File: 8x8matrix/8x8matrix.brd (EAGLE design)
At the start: 60.4 x 60.5 mm, 21 parts

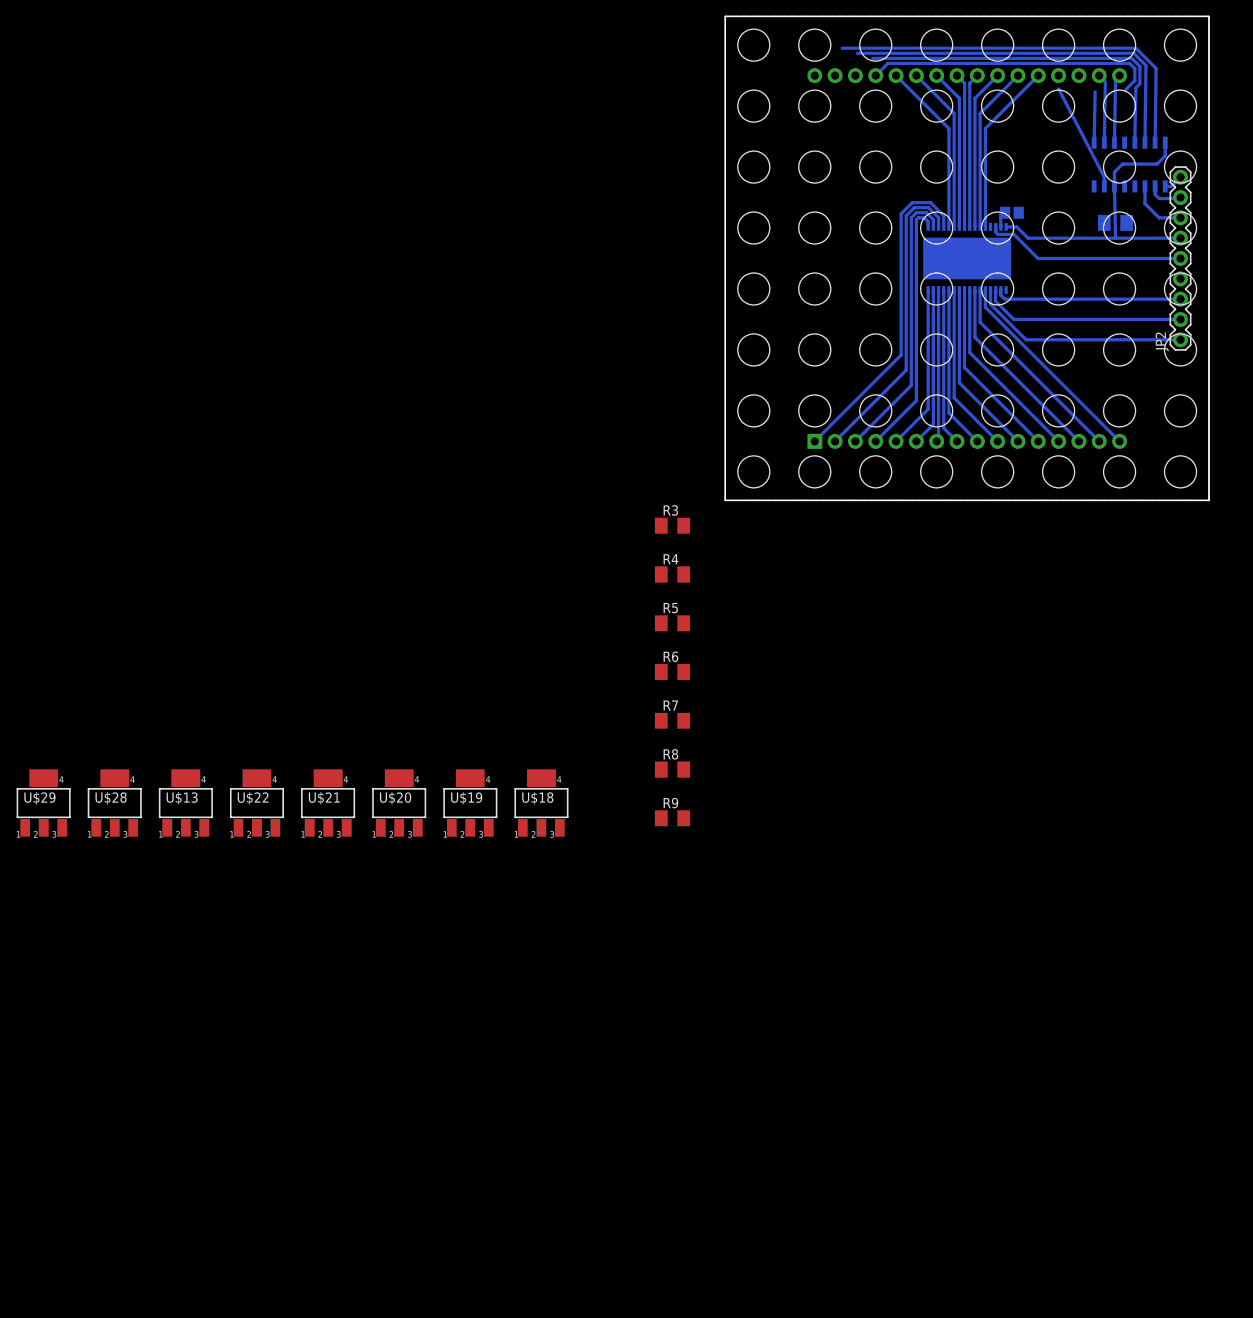
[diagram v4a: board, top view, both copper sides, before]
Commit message: tried with regular SOT23 PNPs
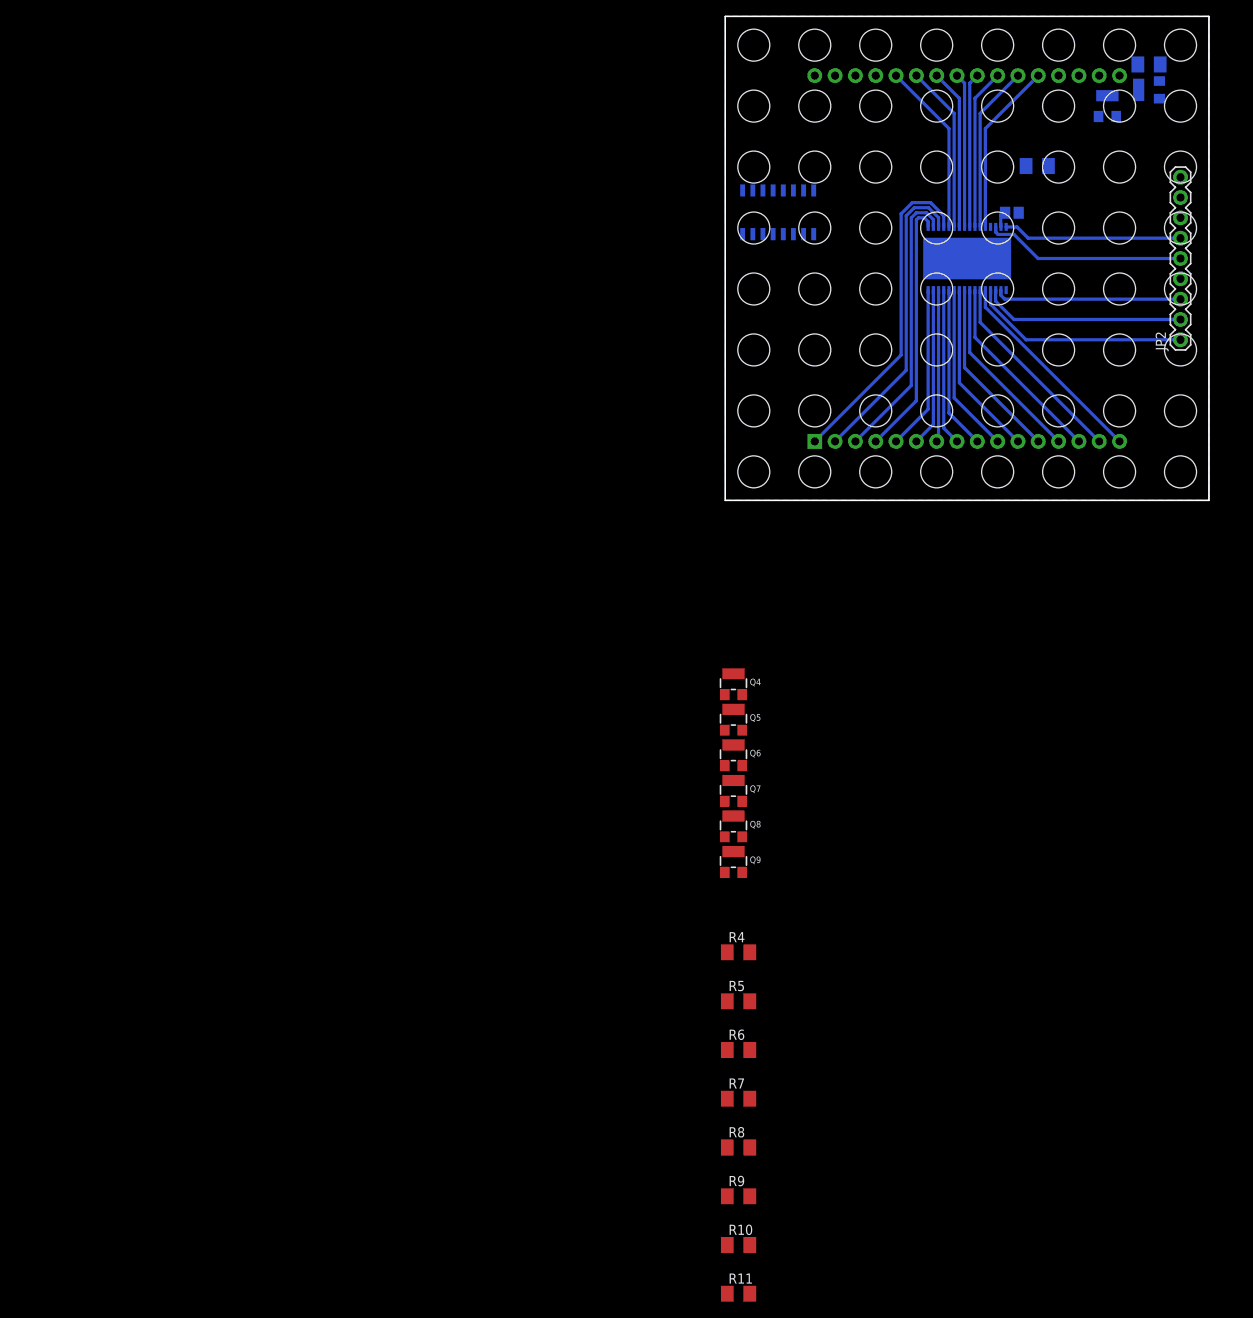
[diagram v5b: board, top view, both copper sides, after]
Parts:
- removed U$13, U$18, U$19, U$20, U$21, U$22, U$28, U$29: FZTA92, mylib:SOT223
- added Q1, Q2, Q4, Q5, Q6, Q7, Q8, Q9: (no value), microbuilder:SOT23-W
- added R10, R11: 0R, resistor:M1206
- moved R3 82.9 mm to (53.0, 54.5), flipped to the bottom, turned to 180 degrees
- moved R9 48.0 mm to (1.65, -87.0)
- moved R4 48.0 mm to (1.65, -56.5)
- moved R5 48.0 mm to (1.65, -62.6)
- moved R7 48.0 mm to (1.65, -74.8)
- moved R8 48.0 mm to (1.65, -80.9)
- moved R6 48.0 mm to (1.65, -68.7)
- moved U$9 44.4 mm to (6.60, 35.9), turned to 180 degrees
- moved R2 12.1 mm to (39.0, 41.8)
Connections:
- new net N$52: Q9.3, U$1.P32
- net 5.0V: now also Q1.2, Q2.2, Q4.2, Q5.2, Q6.2, Q7.2, Q8.2, Q9.2; no longer U$13.3, U$18.3, U$19.3, U$20.3, U$21.3, U$22.3, U$28.3, U$29.3
- net N$25: no longer U$13.1
- net N$26: now also R7.1
- net N$28: now also Q1.3, U$1.P17; no longer R5.2, U$18.1
- net N$29: now also R5.1; no longer R7.1
- net N$30: now also R4.1; no longer R8.1
- net N$31: now also R3.1; no longer R9.1
- net N$32: now also Q4.1, R5.2; no longer U$1.P29, U$13.2, U$13.4
- net N$33: no longer R5.1
- net N$34: now also R10.1; no longer R4.1
- net N$35: now also R11.1; no longer R3.1
- net N$39: now also Q7.1, R9.2; no longer R7.2, U$20.1
- net N$40: now also Q8.1, R10.2; no longer R8.2, U$21.1
- net N$41: now also Q1.1, R3.2; no longer R9.2, U$22.1
- net N$42: now also Q2.1, R4.2; no longer U$1.P30, U$18.2, U$18.4
- net N$43: now also Q5.1, R6.2, R7.2; no longer U$1.P17, U$22.2, U$22.4
- net N$44: now also Q2.3; no longer U$21.2, U$21.4
- net N$45: now also Q6.1, R8.2; no longer R6.2, U$19.1
- net N$46: now also Q9.1, R11.2; no longer U$1.P19, U$20.2, U$20.4
- net N$47: now also Q5.3; no longer U$19.2, U$19.4
- net N$48: now also Q4.3, U$1.P19; no longer R4.2, U$28.1
- net N$49: now also Q6.3, U$1.P29; no longer R3.2, U$29.1
- net N$50: now also Q7.3, U$1.P30; no longer U$1.P31, U$28.2, U$28.4
- net N$51: now also Q8.3, U$1.P31; no longer U$1.P32, U$29.2, U$29.4
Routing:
- net N$35: track 49.6 -> 0.00 mm
- net N$34: track 46.4 -> 0.00 mm
- net N$33: track 43.6 -> 0.00 mm
- net N$32: track 36.4 -> 0.00 mm
- net 5.0V: track 39.5 -> 22.4 mm
- net N$26: track 13.6 -> 0.00 mm
- net N$31: track 7.88 -> 0.00 mm
- net N$30: track 7.62 -> 0.00 mm
- net N$38: track 7.34 -> 0.00 mm
- net N$29: track 6.35 -> 0.00 mm
- net N$37: track 4.45 -> 0.00 mm
- net N$36: track 2.38 -> 0.00 mm

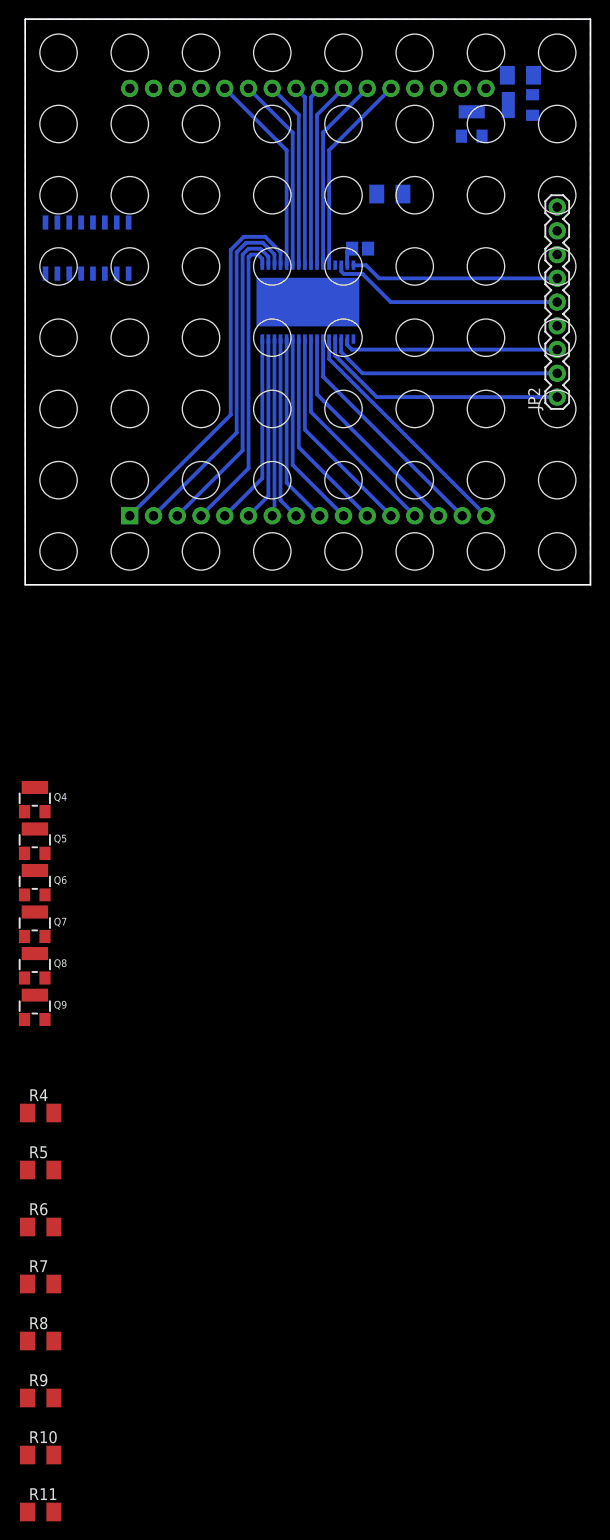
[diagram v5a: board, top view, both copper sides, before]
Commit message: tried with BCR198S pnp arrays
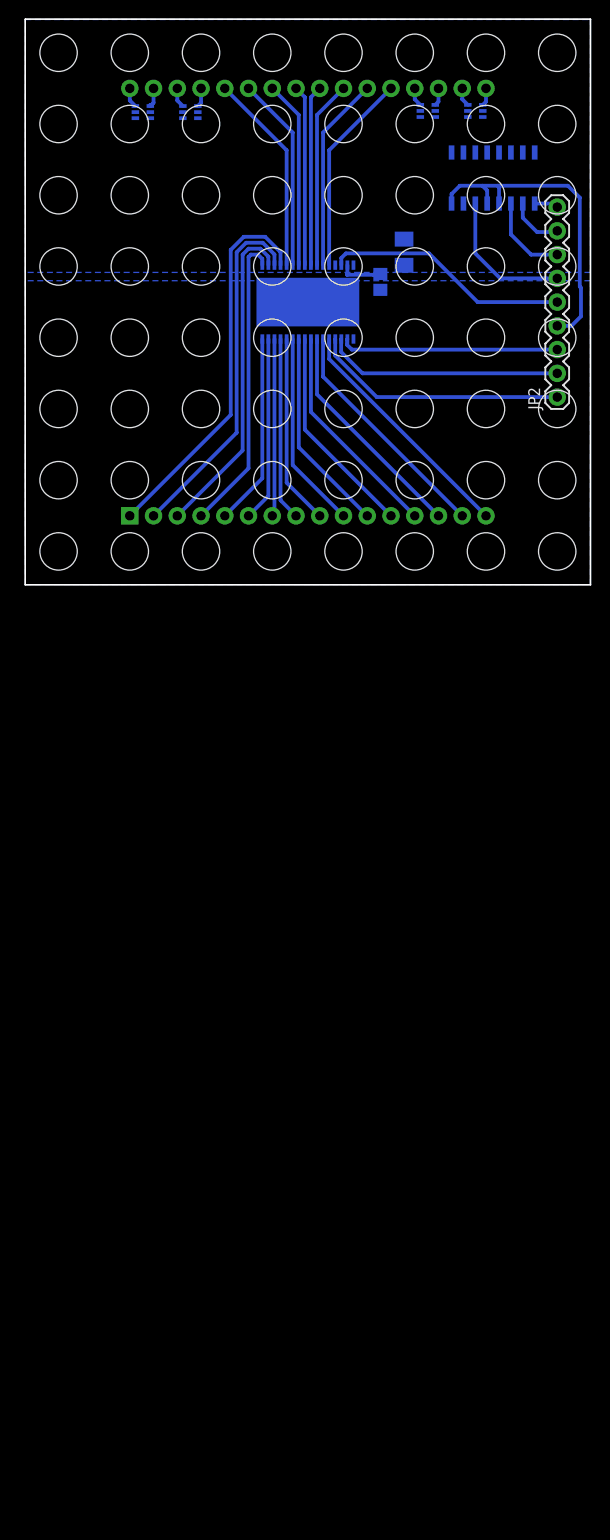
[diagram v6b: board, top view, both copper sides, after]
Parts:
- removed Q1, Q2, Q4, Q5, Q6, Q7, Q8, Q9: (no value), microbuilder:SOT23-W
- removed R10, R11, R3, R4, R5, R6, R7, R8, R9: 0R, resistor:M1206
- added U$13, U$17, U$18, U$19: BCR198S, mylib:SOT363_PHILIPS
- moved U$9 44.1 mm to (50.0, 43.6), turned to 0 degrees
- moved R2 6.41 mm to (40.5, 35.6), turned to 270 degrees
- moved R1 4.16 mm to (38.0, 32.4), turned to 90 degrees
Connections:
- removed net N$42: Q2.1, R4.2
- removed net N$43: Q5.1, R6.2, R7.2
- removed net N$44: Q2.3, U$1.P18
- removed net N$45: Q6.1, R8.2
- removed net N$46: Q9.1, R11.2
- removed net N$48: Q4.3, U$1.P19
- removed net N$49: Q6.3, U$1.P29
- removed net N$51: Q8.3, U$1.P31
- net 5.0V: now also R2.1, R2.2, U$13.1, U$13.6, U$17.1, U$17.6, U$18.1, U$18.6, U$19.6; no longer Q1.2, Q2.2, Q4.2, Q5.2, Q6.2, Q7.2, Q8.2, Q9.2
- net GND: no longer R2.1, R2.2
- net N$25: now also U$18.2
- net N$26: now also U$17.5; no longer R6.1, R7.1
- net N$28: now also U$1.P19, U$17.4; no longer Q1.3, U$1.P17
- net N$29: now also U$17.2; no longer R5.1
- net N$30: now also U$13.5; no longer R4.1
- net N$31: now also U$13.2; no longer R3.1
- net N$32: now also U$1.P18, U$13.3; no longer Q4.1, R5.2
- net N$33: now also U$18.5
- net N$34: now also U$19.2; no longer R10.1
- net N$35: now also U$19.5; no longer R11.1
- net N$39: now also U$1.P17, U$13.4; no longer Q7.1, R9.2
- net N$40: now also U$1.P29, U$18.4; no longer Q8.1, R10.2
- net N$41: now also U$1.P31, U$19.4; no longer Q1.1, R3.2
- net N$47: now also U$17.3; no longer Q5.3
- net N$50: now also U$18.3; no longer Q7.3
- net N$52: now also U$19.3; no longer Q9.3
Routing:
- net GND: track 0.00 -> 35.4 mm
- net N$38: track 0.00 -> 9.15 mm
- net 5.0V: track 22.4 -> 15.2 mm
- net N$37: track 0.00 -> 5.89 mm
- net N$36: track 0.00 -> 2.57 mm
- net N$27: track 2.18 -> 4.60 mm
- net N$41: track 0.00 -> 2.16 mm
- net N$50: track 0.00 -> 2.14 mm
- net N$52: track 0.00 -> 2.14 mm
- net N$40: track 0.00 -> 2.03 mm
- net N$47: track 0.00 -> 2.01 mm
- net N$32: track 0.00 -> 2.01 mm
- net N$39: track 0.00 -> 1.91 mm
- net N$28: track 0.00 -> 1.91 mm
- net XLAT: track 25.1 -> 26.2 mm
- added copper zone on layer 16, net 5.0V

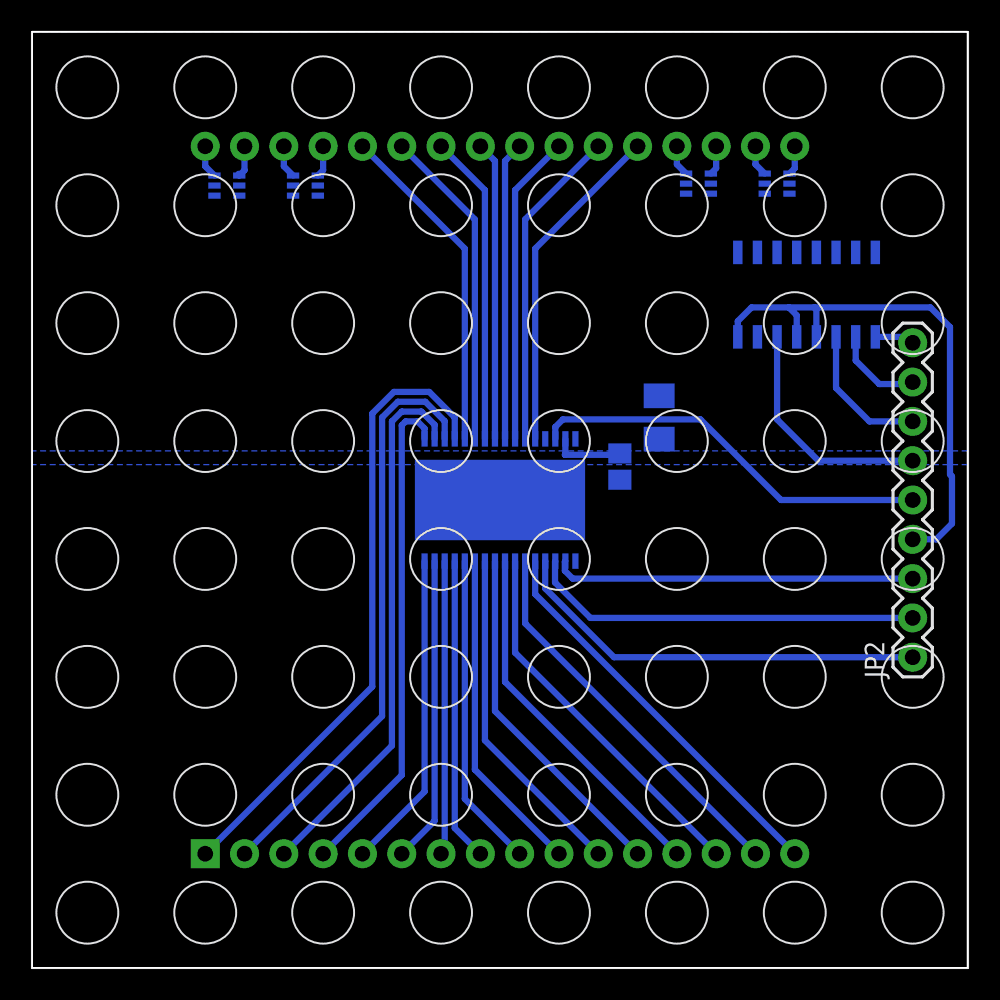
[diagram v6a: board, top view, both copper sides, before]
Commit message: found something that works: IRF7104
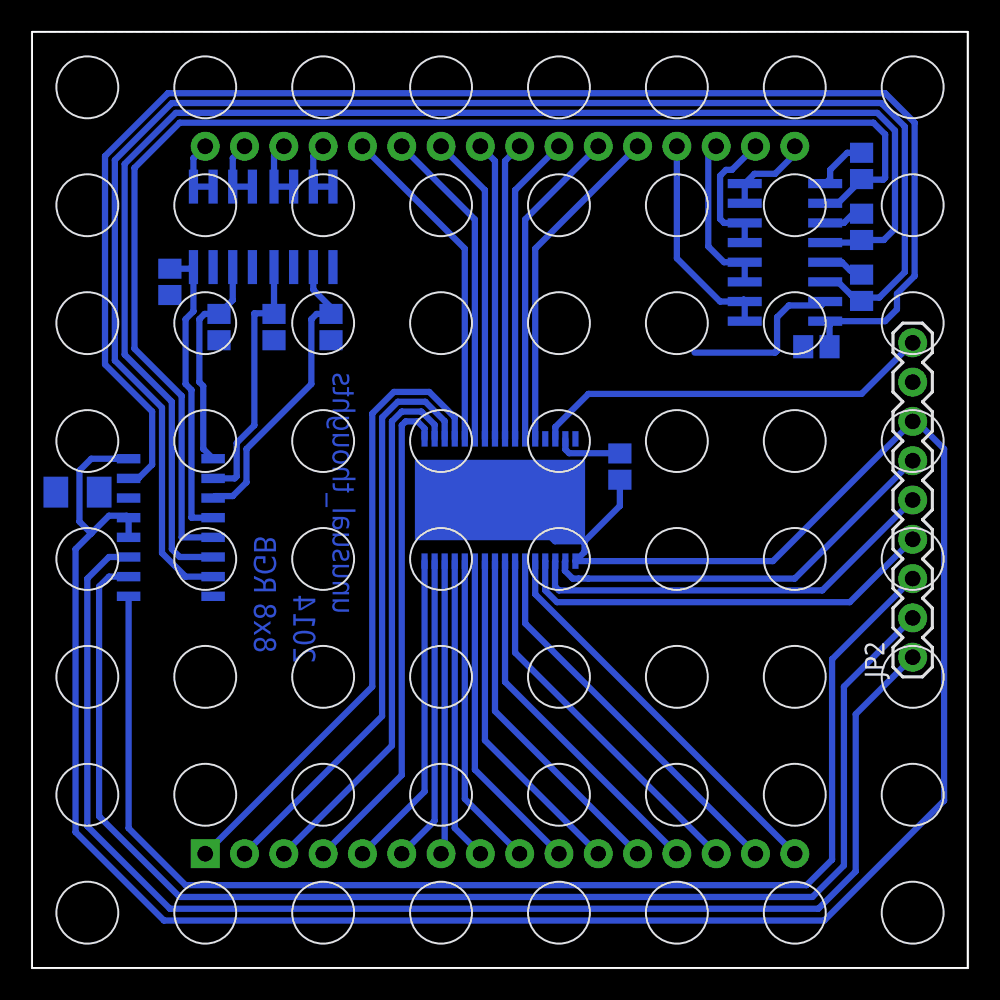
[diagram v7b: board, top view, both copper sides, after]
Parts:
- removed U$13, U$17, U$18, U$19: BCR198S, mylib:SOT363_PHILIPS
- added R10, R3, R4, R5, R6, R7, R8, R9: (no value), resistor:R0805
- added U$28, U$29, U$30, U$31: IRF7104, mylib:SOIC8
- R1: value (none) -> 3.3k
- moved U$9 43.7 mm to (9.02, 28.4), turned to 90 degrees
- moved R2 37.9 mm to (2.92, 30.7), turned to 180 degrees
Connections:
- removed net N$25: U$18.2, U$9.12
- removed net N$26: U$17.5, U$9.7
- removed net N$29: U$17.2, U$9.9
- removed net N$30: U$13.5, U$9.10
- removed net N$31: U$13.2, U$9.11
- removed net N$33: U$18.5, U$9.13
- removed net N$34: U$19.2, U$9.14
- removed net N$35: U$19.5, U$9.15
- removed net N$47: U$1.P20, U$17.3
- new net N$42: U$1.P20, U$29.5, U$29.6
- new net Y0: R5.1, U$29.2, U$9.15
- new net Y1: R4.1, U$28.4, U$9.14
- new net Y2: R3.1, U$28.2, U$9.13
- new net Y3: R10.1, U$31.4, U$9.12
- new net Y4: R7.1, U$30.2, U$9.11
- new net Y5: R8.1, U$30.4, U$9.10
- new net Y6: R9.1, U$31.2, U$9.9
- new net Y7: R6.1, U$29.4, U$9.7
- net 5.0V: now also JP2.8, R10.2, R3.2, R4.2, R5.2, R6.2, R7.2, R8.2, R9.2, U$28.1, U$28.3, U$29.1, U$29.3, U$30.1, U$30.3, U$31.1, U$31.3; no longer JP2.6, U$13.1, U$13.6, U$17.1, U$17.6, U$18.1, U$18.6, U$19.6
- net BLANK: now also JP2.6; no longer JP2.3
- net GND: now also JP2.7; no longer JP2.4
- net N$28: now also U$29.7, U$29.8; no longer U$17.4
- net N$32: now also U$28.5, U$28.6; no longer U$13.3
- net N$36: now also JP2.3; no longer JP2.9
- net N$37: now also JP2.2; no longer JP2.8
- net N$38: now also JP2.1; no longer JP2.7
- net N$39: now also U$28.7, U$28.8; no longer U$13.4
- net N$40: now also U$30.7, U$30.8; no longer U$18.4
- net N$41: now also U$31.7, U$31.8; no longer U$19.4
- net N$50: now also U$30.5, U$30.6; no longer U$18.3
- net N$52: now also U$31.5, U$31.6; no longer U$19.3
- net SCLK: now also JP2.5; no longer JP2.2
- net SIN: now also JP2.4; no longer JP2.1
- net XLAT: now also JP2.9; no longer JP2.5
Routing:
- net GND: track 35.4 -> 158.5 mm
- net Y0: track 0.00 -> 99.7 mm
- net Y7: track 0.00 -> 97.2 mm
- net Y1: track 0.00 -> 91.9 mm
- net Y2: track 0.00 -> 84.5 mm
- net N$36: track 2.57 -> 83.0 mm
- net N$37: track 5.89 -> 86.0 mm
- net N$38: track 9.15 -> 87.5 mm
- net Y4: track 0.00 -> 20.3 mm
- net Y3: track 0.00 -> 19.7 mm
- net Y5: track 0.00 -> 16.9 mm
- net Y6: track 0.00 -> 14.2 mm
- net N$42: track 0.00 -> 14.2 mm
- net N$28: track 1.91 -> 10.7 mm
- net N$32: track 2.01 -> 8.84 mm
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- removed copper zone on layer 16, net GND
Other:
- board text added: "2014"
- board text added: "8x8 RGB"
- board text added: "unusual_thoughts"

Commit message: changed 238 to 138
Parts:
- U$9: value CD74HC238M -> 74HC138D
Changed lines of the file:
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@@
 <element name="U$14" library="TLC5947" package="HTSSOP32DAP" value="TLC5947DAP" x="30.226" y="30.226" rot="MR0"/>
 <element name="R1" library="resistor" package="R0805" value="3.3k" x="37.973" y="32.385" rot="MR90"/>
-<element name="U$9" library="mylib" package="SO-16" value="CD74HC238M" x="9.017" y="28.448" rot="MR90"/>
+<element name="U$9" library="mylib" package="SO-16" value="74HC138D" x="9.017" y="28.448" rot="MR90"/>
 <element name="JP2" library="SparkFun-Connectors" package="1X09" value="M09" x="56.896" y="20.066" rot="R90"/>
 <element name="R2" library="resistor" package="M1206" value="0R" x="2.921" y="30.734" rot="MR180"/>
